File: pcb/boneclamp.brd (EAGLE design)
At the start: 160 x 100 mm, 10 parts, among them U1 AD7656YSTZ, U2 AD5754RBREZ, U3 SN74ABT541BDW, X1 F15-SHEILD

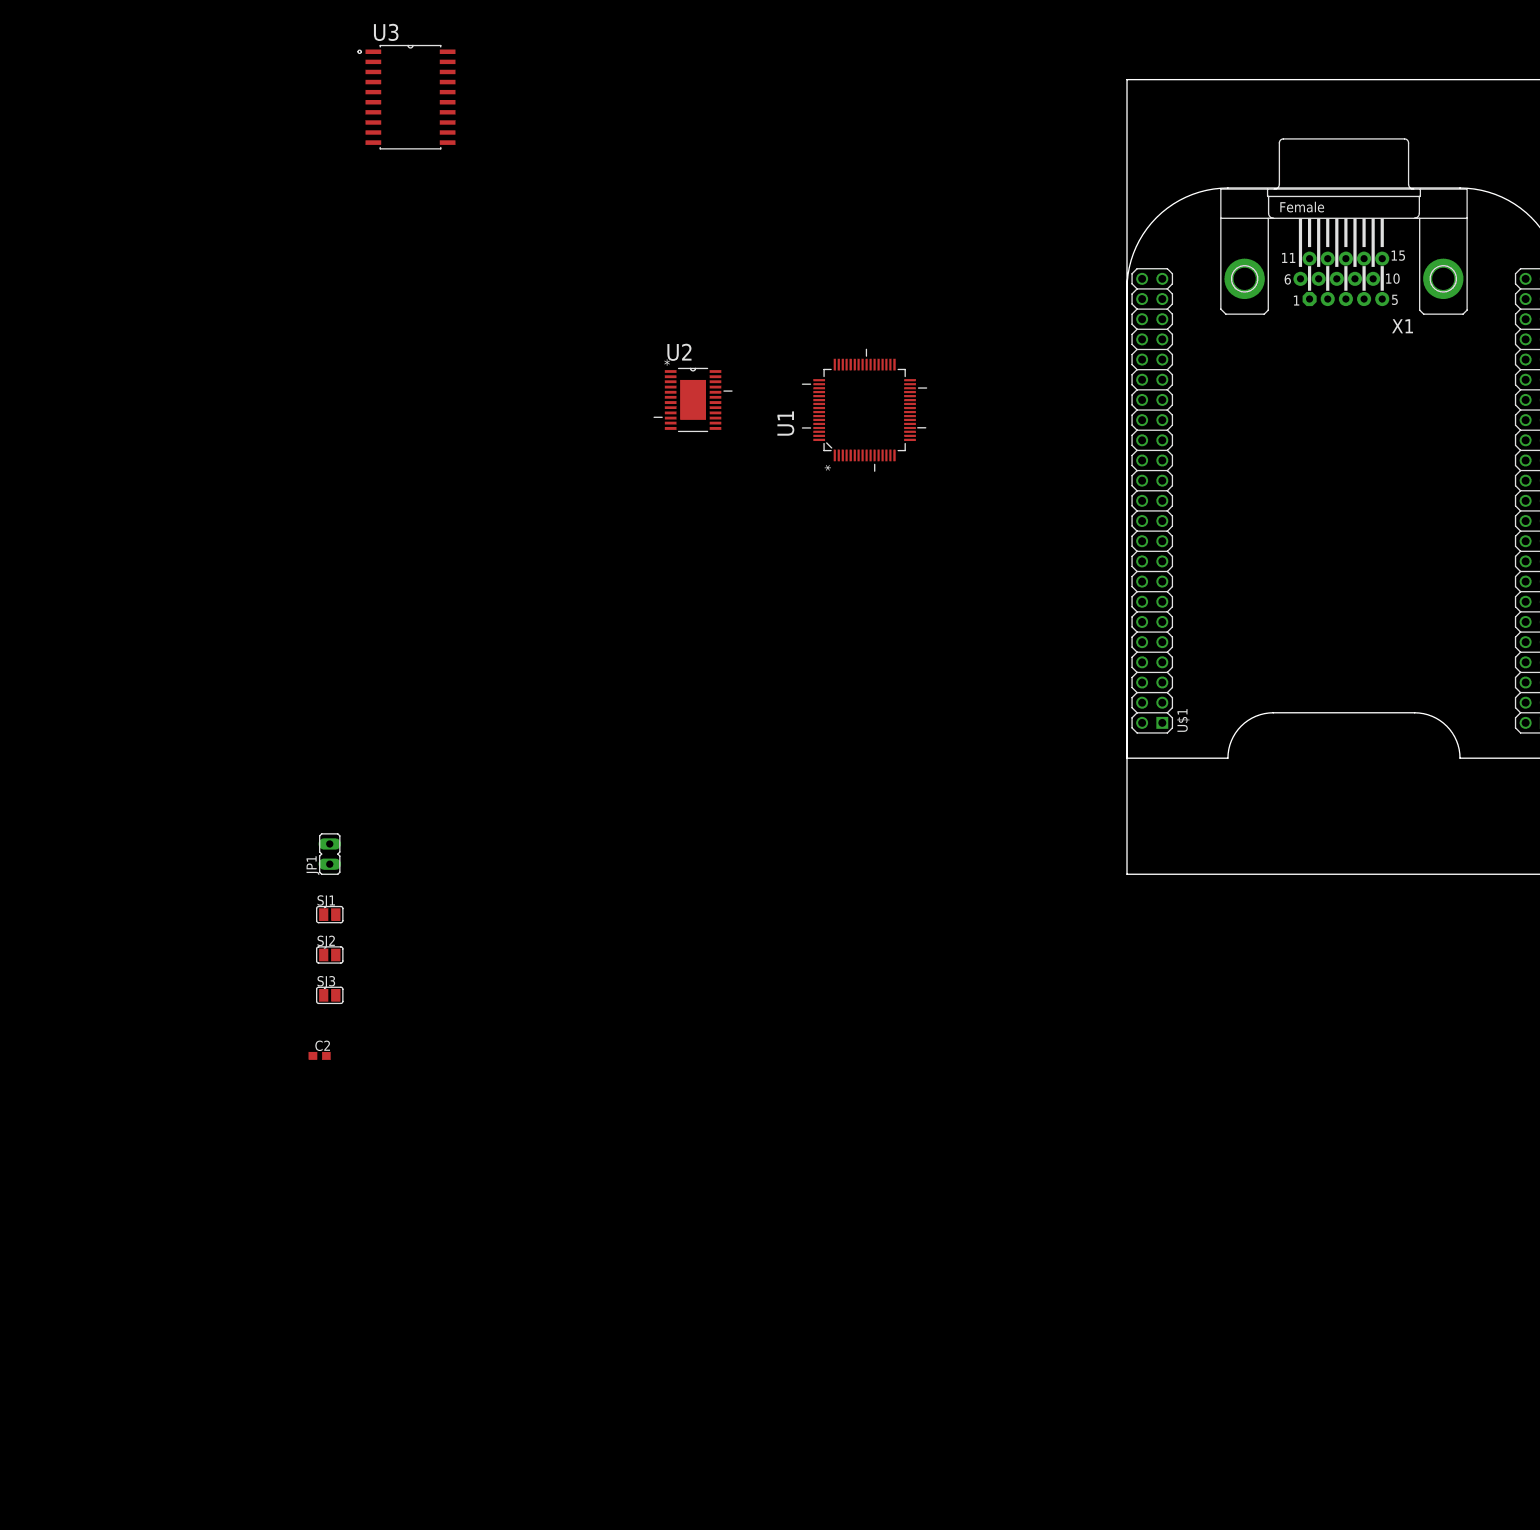
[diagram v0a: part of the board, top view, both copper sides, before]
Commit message: Started working through the basic wiring on the schematic, connectrating on grounds, power, and analog IO
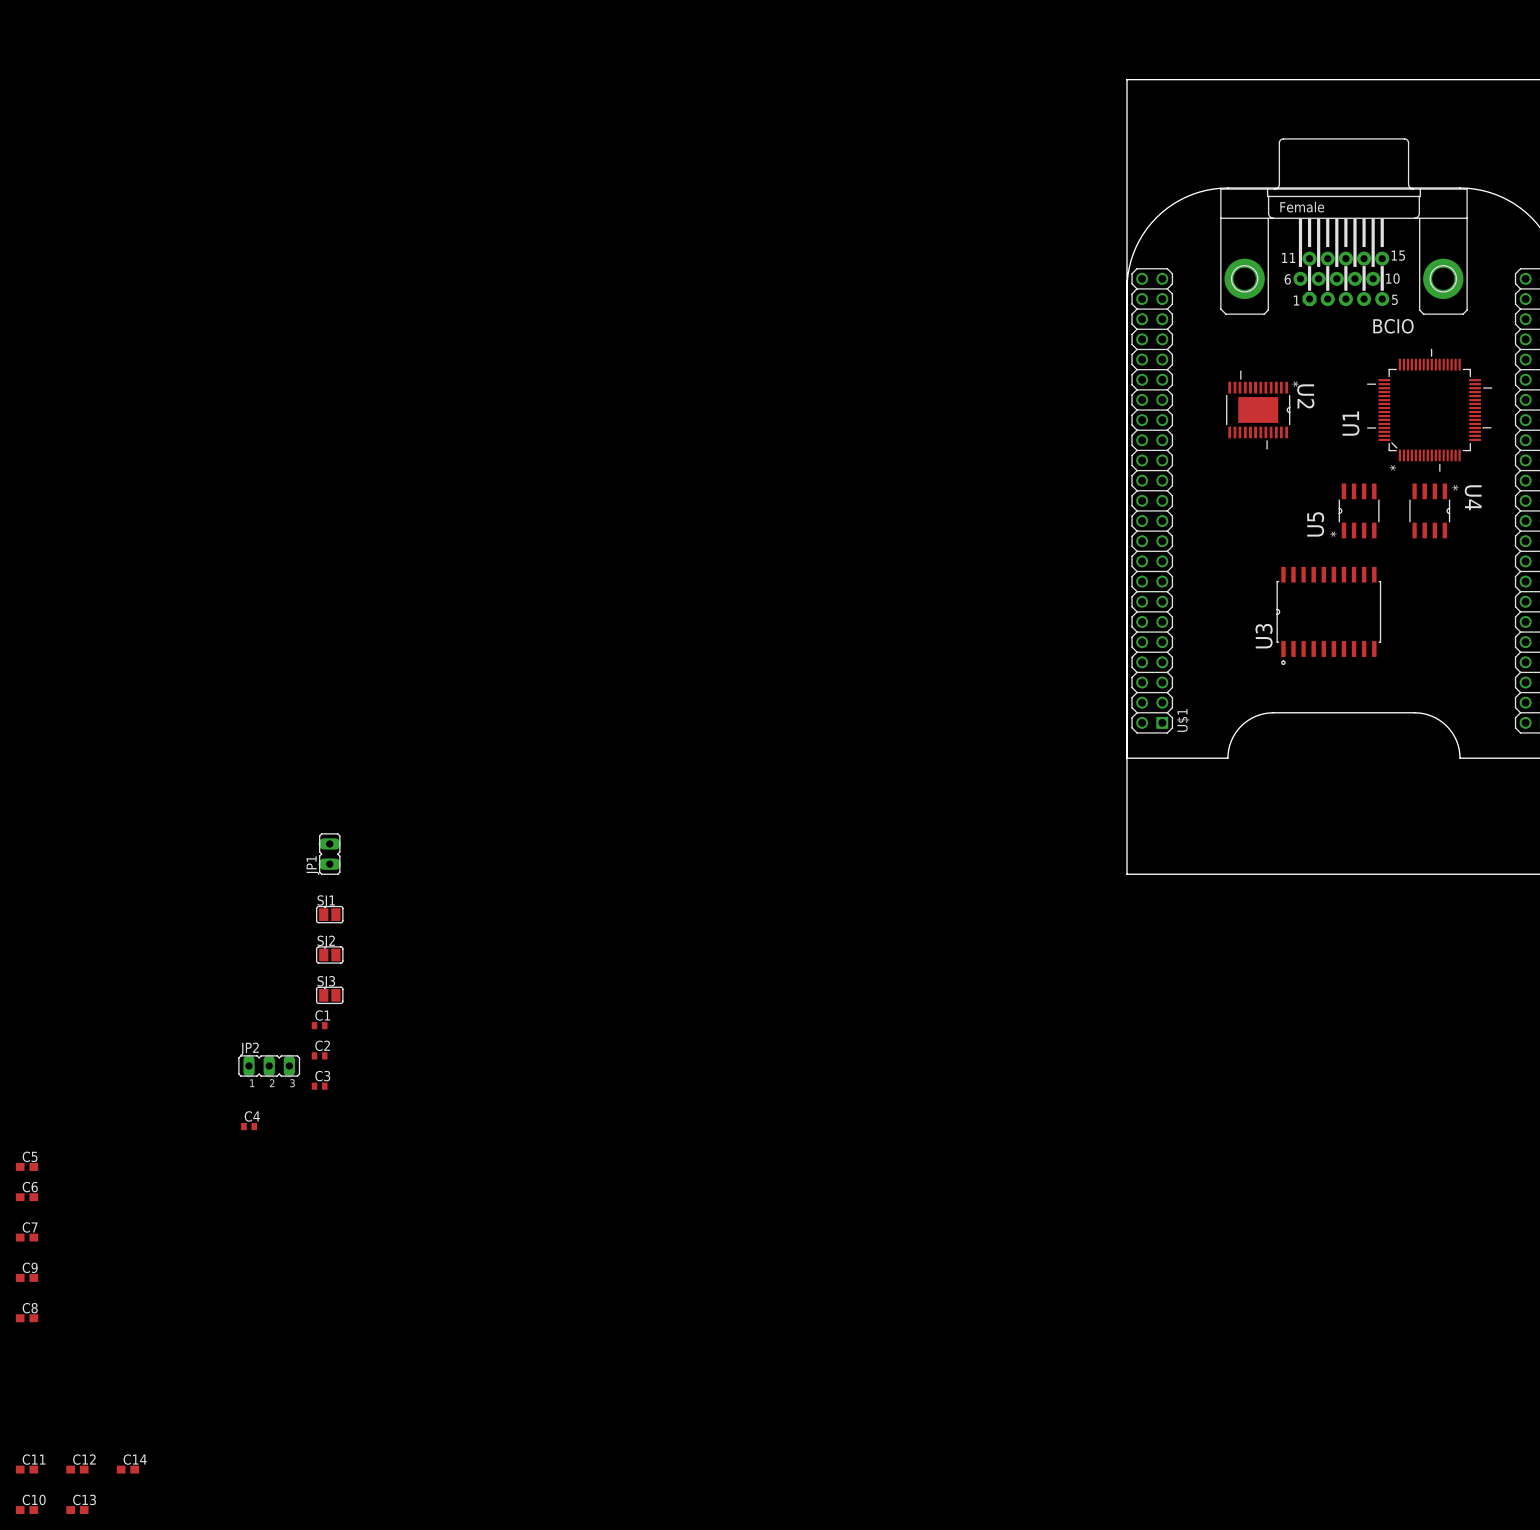
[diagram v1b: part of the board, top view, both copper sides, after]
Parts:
- added C1, C3, C4: 1 uF, rcl:C0402
- added C10, C13, C5, C8: 10uF, rcl:C0603
- added C11, C12, C14, C6, C7, C9: 0.1uF, rcl:C0603
- added JP2: (no value), jumper:JP2
- added U4, U5: ADP3303ARZ-5, analog-devices-01:SOIC127P600X175-8N
- C2: value (none) -> 1 uF; device rcl:C0603 -> rcl:C0402
- moved U3 132.5 mm to (25.4, 33.0), turned to 90 degrees
- moved U2 71.1 mm to (16.5, 58.4), turned to 270 degrees
- moved U1 71.1 mm to (38.1, 58.4)
- renumbered X1 to BCIO
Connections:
- removed net AVCC_2: U1.46
- removed net AVCC_3: U1.47
- removed net AVCC_4: U1.60
- removed net AVCC_5: U1.40
- removed net AVCC_6: U1.50
- removed net AVCC_7: U1.41
- removed net AVCC_8: U1.34
- removed net GND: U$1.1, U$1.2, U$1.47, U$1.48, U$1.89, U$1.90, U$1.91, U$1.92
- removed net SYS_5V: U$1.53
- new net BB_5V: C10.1, C11.1, C5.1, C6.1, U$1.53, U4.5, U4.7, U4.8, U5.5, U5.7, U5.8
- new net CONVST: U1.21, U1.22, U1.23
- new net DGND: C10.2, C11.2, C13.2, C14.2, JP2.3, U$1.92, U1.25, U1.8
- new net N$10: C2.1, U1.56
- new net N$11: C1.1, U1.58
- new net N$12: JP2.2, U1.27
- new net N$13: C4.1, U1.34, U1.35, U1.40, U1.41, U1.46, U1.47, U1.50, U1.60
- new net N$15: C12.2, U5.3
- new net N$16: C7.2, U4.3
- new net N$9: C3.1
- new net VDD_BB: U$1.51
- new net VDRIVE: JP2.1, U$1.49
- net AGND: now also C1.2, C2.2, C3.2, C4.2, C5.2, C6.2, C8.2, C9.2, U$1.1, U$1.2, U$1.47, U$1.48, U$1.89, U$1.90, U$1.91, U1.32, U1.37, U1.38, U1.43, U1.44, U1.49, U1.52, U1.53, U1.57, U1.59, U4.4, U5.4
- net AVCC: now also C7.1, C8.1, C9.1, U4.1, U4.2; no longer U1.35
- net DVCC: now also C12.1, C13.1, C14.1, U5.1, U5.2
- net VDD_3V3EXP: no longer U$1.49
- net VDD_5V: no longer U$1.51

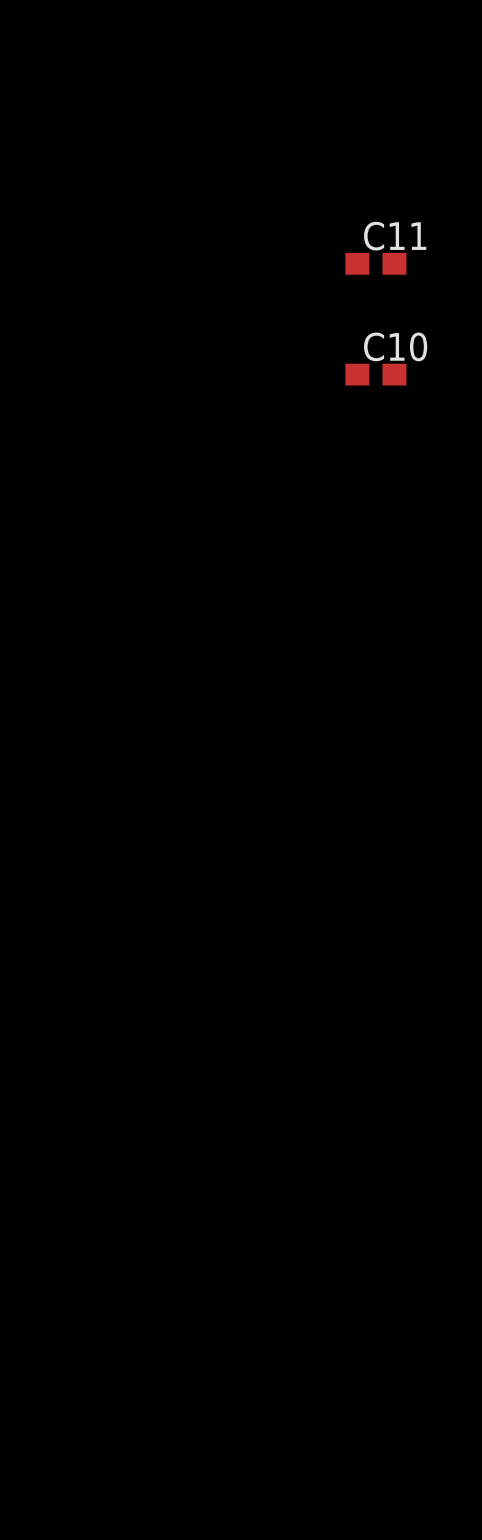
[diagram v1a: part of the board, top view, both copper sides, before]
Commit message: Added optional compensation comoponents and test points to DAC output lines. Added a right angle 0.1 inch pitch header for outside power input.
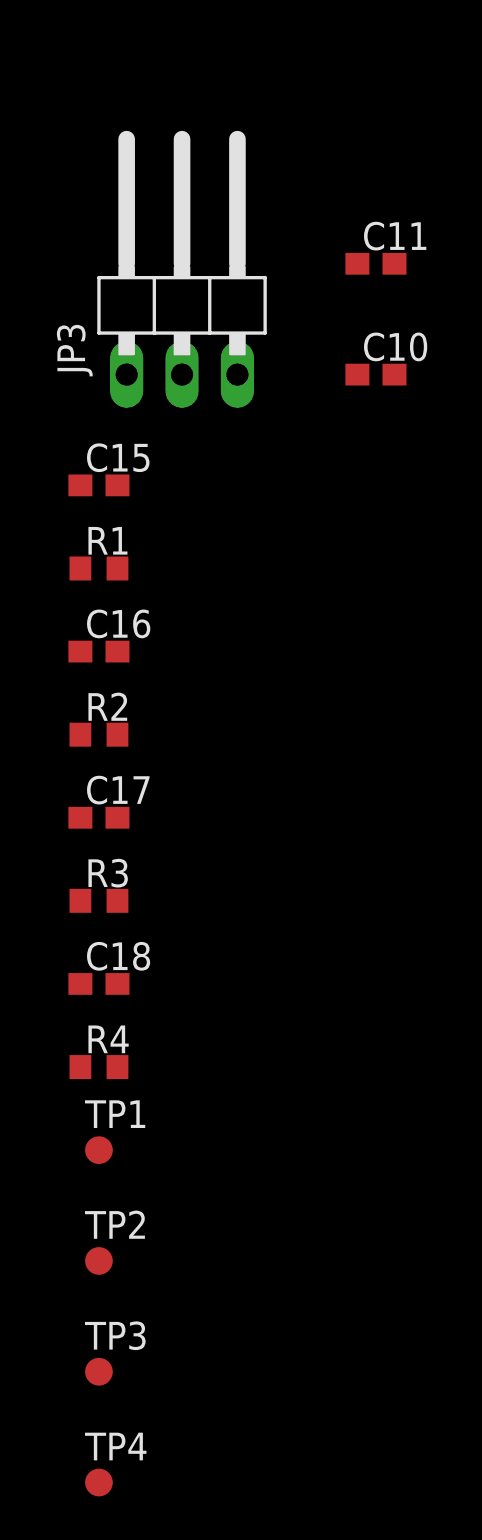
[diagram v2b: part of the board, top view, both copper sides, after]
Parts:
- added C15, C16, C17, C18: (no value), rcl:C0603
- added JP3: (no value), pinhead:1X03/90
- added R1, R2, R3, R4: (no value), rcl:R0603
- added TP1, TP2, TP3, TP4: TPB1,27, testpad:B1,27
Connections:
- removed net AVDD: U2.24
- removed net AVSS: U2.1
- new net N$17: C15.2, R1.1
- net AGND: now also C16.2, C17.2, C18.2, R2.1, R3.1, R4.1
- net DAC_A: now also C18.1, R4.2, TP1.TP
- net DAC_B: now also C17.1, R3.2, TP2.TP
- net DAC_C: now also C16.1, R2.2, TP3.TP
- net DAC_D: now also C15.1, R1.2, TP4.TP
- net VDD: now also U2.24
- net VSS: now also U2.1
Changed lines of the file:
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@@
 <element name="C13" library="rcl" package="C0603" value="10uF" x="-132.08" y="-80.01"/>
 <element name="C14" library="rcl" package="C0603" value="0.1uF" x="-125.73" y="-74.93"/>
+<element name="JP3" library="pinhead" package="1X03/90" value="" x="-147.32" y="-76.2"/>
+<element name="C15" library="rcl" package="C0603" value="" x="-151.13" y="-85.09"/>
+<element name="R1" library="rcl" package="R0603" value="" x="-151.13" y="-88.9"/>
+<element name="C16" library="rcl" package="C0603" value="" x="-151.13" y="-92.71"/>
+<element name="R2" library="rcl" package="R0603" value="" x="-151.13" y="-96.52"/>
+<element name="C17" library="rcl" package="C0603" value="" x="-151.13" y="-100.33"/>
+<element name="R3" library="rcl" package="R0603" value="" x="-151.13" y="-104.14"/>
+<element name="C18" library="rcl" package="C0603" value="" x="-151.13" y="-107.95"/>
+<element name="R4" library="rcl" package="R0603" value="" x="-151.13" y="-111.76"/>
+<element name="TP1" library="testpad" package="B1,27" value="TPB1,27" x="-151.13" y="-115.57">
+<attribute name="TP_SIGNAL_NAME" value="" x="-151.13" y="-115.57" size="1.778" layer="27" display="off"/>
+</element>
+<element name="TP2" library="testpad" package="B1,27" value="TPB1,27" x="-151.13" y="-120.65">
+<attribute name="TP_SIGNAL_NAME" value="" x="-151.13" y="-120.65" size="1.778" layer="27" display="off"/>
+</element>
+<element name="TP3" library="testpad" package="B1,27" value="TPB1,27" x="-151.13" y="-125.73">
+<attribute name="TP_SIGNAL_NAME" value="" x="-151.13" y="-125.73" size="1.778" layer="27" display="off"/>
+</element>
+<element name="TP4" library="testpad" package="B1,27" value="TPB1,27" x="-151.13" y="-130.81">
+<attribute name="TP_SIGNAL_NAME" value="" x="-151.13" y="-130.81" size="1.778" layer="27" display="off"/>
+</element>
 </elements>
 <signals>
@@
 <signal name="VDD">
 <contactref element="U1" pad="31"/>
+<contactref element="U2" pad="24"/>
+<wire x1="20.0914" y1="55.6006" x2="43.815" y2="61.6712" width="0" layer="19" extent="1-1"/>
 </signal>
 <signal name="DVCC">
 <contactref element="U1" pad="26"/>
-<contactref element="U2" pad="14"/>
 <contactref element="C13" pad="1"/>
 <contactref element="C14" pad="1"/>
@@
 <contactref element="U5" pad="2"/>
 <contactref element="C12" pad="1"/>
+<contactref element="U2" pad="14"/>
 <wire x1="-132.93" y1="-74.93" x2="-132.93" y2="-80.01" width="0" layer="19" extent="1-1"/>
 <wire x1="-126.58" y1="-74.93" x2="-132.93" y2="-74.93" width="0" layer="19" extent="1-1"/>
-<wire x1="28.575" y1="43.2562" x2="-132.93" y2="-74.93" width="0" layer="19" extent="1-1"/>
-<wire x1="27.305" y1="43.2562" x2="28.575" y2="43.2562" width="0" layer="19" extent="1-1"/>
-<wire x1="13.589" y1="55.6006" x2="27.305" y2="43.2562" width="0" layer="19" extent="1-1"/>
-<wire x1="43.815" y1="59.182" x2="13.589" y2="55.6006" width="0" layer="19" extent="1-1"/>
-</signal>
-<signal name="AVDD">
-<contactref element="U2" pad="24"/>
-</signal>
-<signal name="AVSS">
-<contactref element="U2" pad="1"/>
+<wire x1="13.589" y1="55.6006" x2="-126.58" y2="-74.93" width="0" layer="19" extent="1-1"/>
+<wire x1="27.305" y1="43.2562" x2="13.589" y2="55.6006" width="0" layer="19" extent="1-1"/>
+<wire x1="28.575" y1="43.2562" x2="27.305" y2="43.2562" width="0" layer="19" extent="1-1"/>
+<wire x1="43.815" y1="59.182" x2="28.575" y2="43.2562" width="0" layer="19" extent="1-1"/>
 </signal>
 <signal name="EPAD">
@@
 <contactref element="BCIO" pad="8"/>
 <contactref element="U2" pad="3"/>
-<wire x1="26.405" y1="74.93" x2="18.796" y2="61.2394" width="0" layer="19" extent="1-1"/>
+<contactref element="R4" pad="2"/>
+<contactref element="C18" pad="1"/>
+<contactref element="TP1" pad="TP"/>
+<wire x1="18.796" y1="61.2394" x2="26.405" y2="74.93" width="0" layer="19" extent="1-1"/>
+<wire x1="-151.98" y1="-107.95" x2="18.796" y2="61.2394" width="0" layer="19" extent="1-1"/>
+<wire x1="-150.28" y1="-111.76" x2="-151.98" y2="-107.95" width="0" layer="19" extent="1-1"/>
+<wire x1="-151.13" y1="-115.57" x2="-150.28" y2="-111.76" width="0" layer="19" extent="1-1"/>
 </signal>
 <signal name="DAC_B">
 <contactref element="BCIO" pad="9"/>
 <contactref element="U2" pad="4"/>
+<contactref element="TP2" pad="TP"/>
+<contactref element="R3" pad="2"/>
+<contactref element="C17" pad="1"/>
+<wire x1="-150.28" y1="-104.14" x2="-151.98" y2="-100.33" width="0" layer="19" extent="1-1"/>
+<wire x1="-151.13" y1="-120.65" x2="-150.28" y2="-104.14" width="0" layer="19" extent="1-1"/>
+<wire x1="18.1356" y1="61.2394" x2="-151.98" y2="-100.33" width="0" layer="19" extent="1-1"/>
 <wire x1="28.691" y1="74.93" x2="18.1356" y2="61.2394" width="0" layer="19" extent="1-1"/>
 </signal>
 <signal name="DAC_C">
 <contactref element="BCIO" pad="10"/>
+<contactref element="R2" pad="2"/>
+<contactref element="C16" pad="1"/>
 <contactref element="U2" pad="23"/>
+<contactref element="TP3" pad="TP"/>
+<wire x1="-151.98" y1="-92.71" x2="-150.28" y2="-96.52" width="0" layer="19" extent="1-1"/>
+<wire x1="-151.13" y1="-125.73" x2="-150.28" y2="-96.52" width="0" layer="19" extent="1-1"/>
+<wire x1="19.431" y1="55.6006" x2="-151.98" y2="-92.71" width="0" layer="19" extent="1-1"/>
 <wire x1="30.977" y1="74.93" x2="19.431" y2="55.6006" width="0" layer="19" extent="1-1"/>
 </signal>
@@
 <contactref element="BCIO" pad="11"/>
 <contactref element="U2" pad="22"/>
+<contactref element="R1" pad="2"/>
+<contactref element="C15" pad="1"/>
+<contactref element="TP4" pad="TP"/>
+<wire x1="-151.98" y1="-85.09" x2="-150.28" y2="-88.9" width="0" layer="19" extent="1-1"/>
+<wire x1="-151.13" y1="-130.81" x2="-150.28" y2="-88.9" width="0" layer="19" extent="1-1"/>
+<wire x1="18.796" y1="55.6006" x2="-151.98" y2="-85.09" width="0" layer="19" extent="1-1"/>
 <wire x1="22.976" y1="77.47" x2="18.796" y2="55.6006" width="0" layer="19" extent="1-1"/>
 </signal>
@@
 <contactref element="C8" pad="2"/>
 <contactref element="U5" pad="4"/>
+<contactref element="R4" pad="1"/>
+<contactref element="C18" pad="2"/>
+<contactref element="R3" pad="1"/>
+<contactref element="C17" pad="2"/>
+<contactref element="R2" pad="1"/>
+<contactref element="C16" pad="2"/>
+<wire x1="-151.98" y1="-96.52" x2="-150.28" y2="-100.33" width="0" layer="19" extent="1-1"/>
+<wire x1="-150.28" y1="-92.71" x2="-151.98" y2="-96.52" width="0" layer="19" extent="1-1"/>
+<wire x1="-151.98" y1="-104.14" x2="-150.28" y2="-100.33" width="0" layer="19" extent="1-1"/>
+<wire x1="-150.28" y1="-107.95" x2="-151.98" y2="-104.14" width="0" layer="19" extent="1-1"/>
+<wire x1="-151.98" y1="-111.76" x2="-150.28" y2="-107.95" width="0" layer="19" extent="1-1"/>
+<wire x1="-137.58" y1="-55.88" x2="-150.28" y2="-92.71" width="0" layer="19" extent="1-1"/>
 <wire x1="-137.58" y1="-50.8" x2="-137.58" y2="-55.88" width="0" layer="19" extent="1-1"/>
 <wire x1="-137.58" y1="-40.64" x2="-137.58" y2="-50.8" width="0" layer="19" extent="1-1"/>
@@
 <signal name="VSS">
 <contactref element="U1" pad="30"/>
+<contactref element="U2" pad="1"/>
+<wire x1="20.0914" y1="61.2394" x2="43.815" y2="61.1632" width="0" layer="19" extent="1-1"/>
 </signal>
 <signal name="CONVST">
@@
 <wire x1="29.845" y1="43.2562" x2="-131.23" y2="-74.93" width="0" layer="19" extent="1-1"/>
 </signal>
+<signal name="N$17">
+<contactref element="R1" pad="1"/>
+<contactref element="C15" pad="2"/>
+<wire x1="-150.28" y1="-85.09" x2="-151.98" y2="-88.9" width="0" layer="19" extent="1-1"/>
+</signal>
 </signals>
